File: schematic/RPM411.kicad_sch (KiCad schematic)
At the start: 88 parts, among them J1 02x08_tbd, P1 P_Cap, Q1 tbd (GDS), U1 STM32F100C8Tb8, U2 TS5A9411, U3 TS5A9411, U4 TS5A9411, U5 74LVC3G04, U6 74LVC1G32, U7 TLV70030DDC

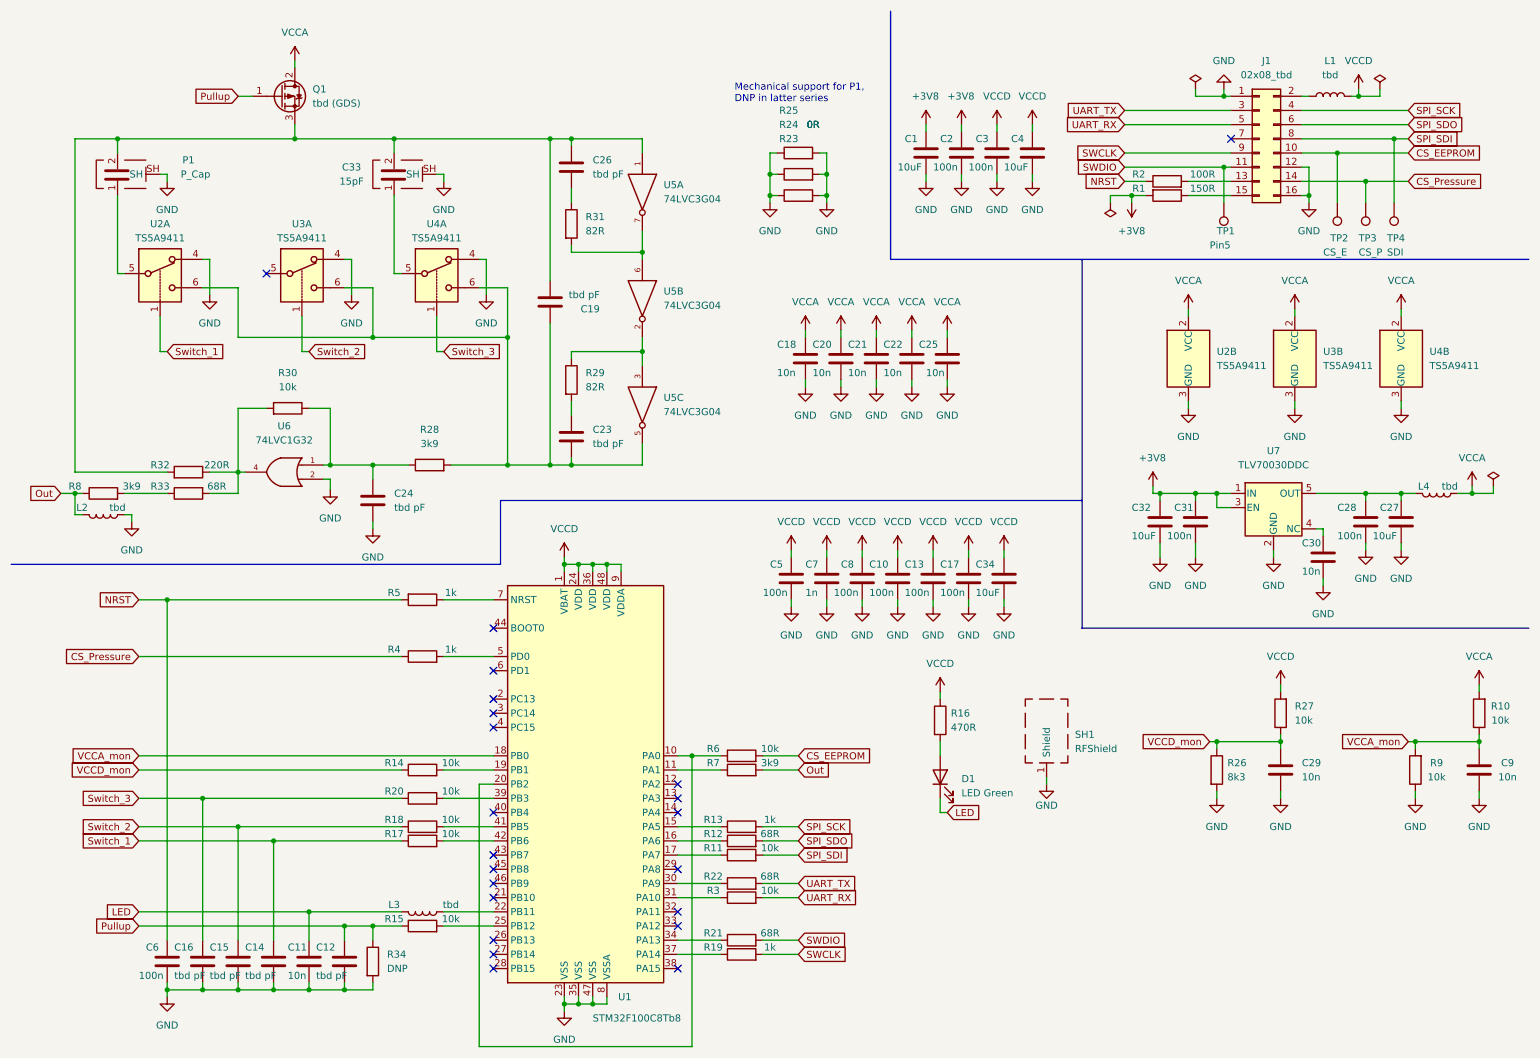
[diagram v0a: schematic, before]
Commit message: renamed CS Signals
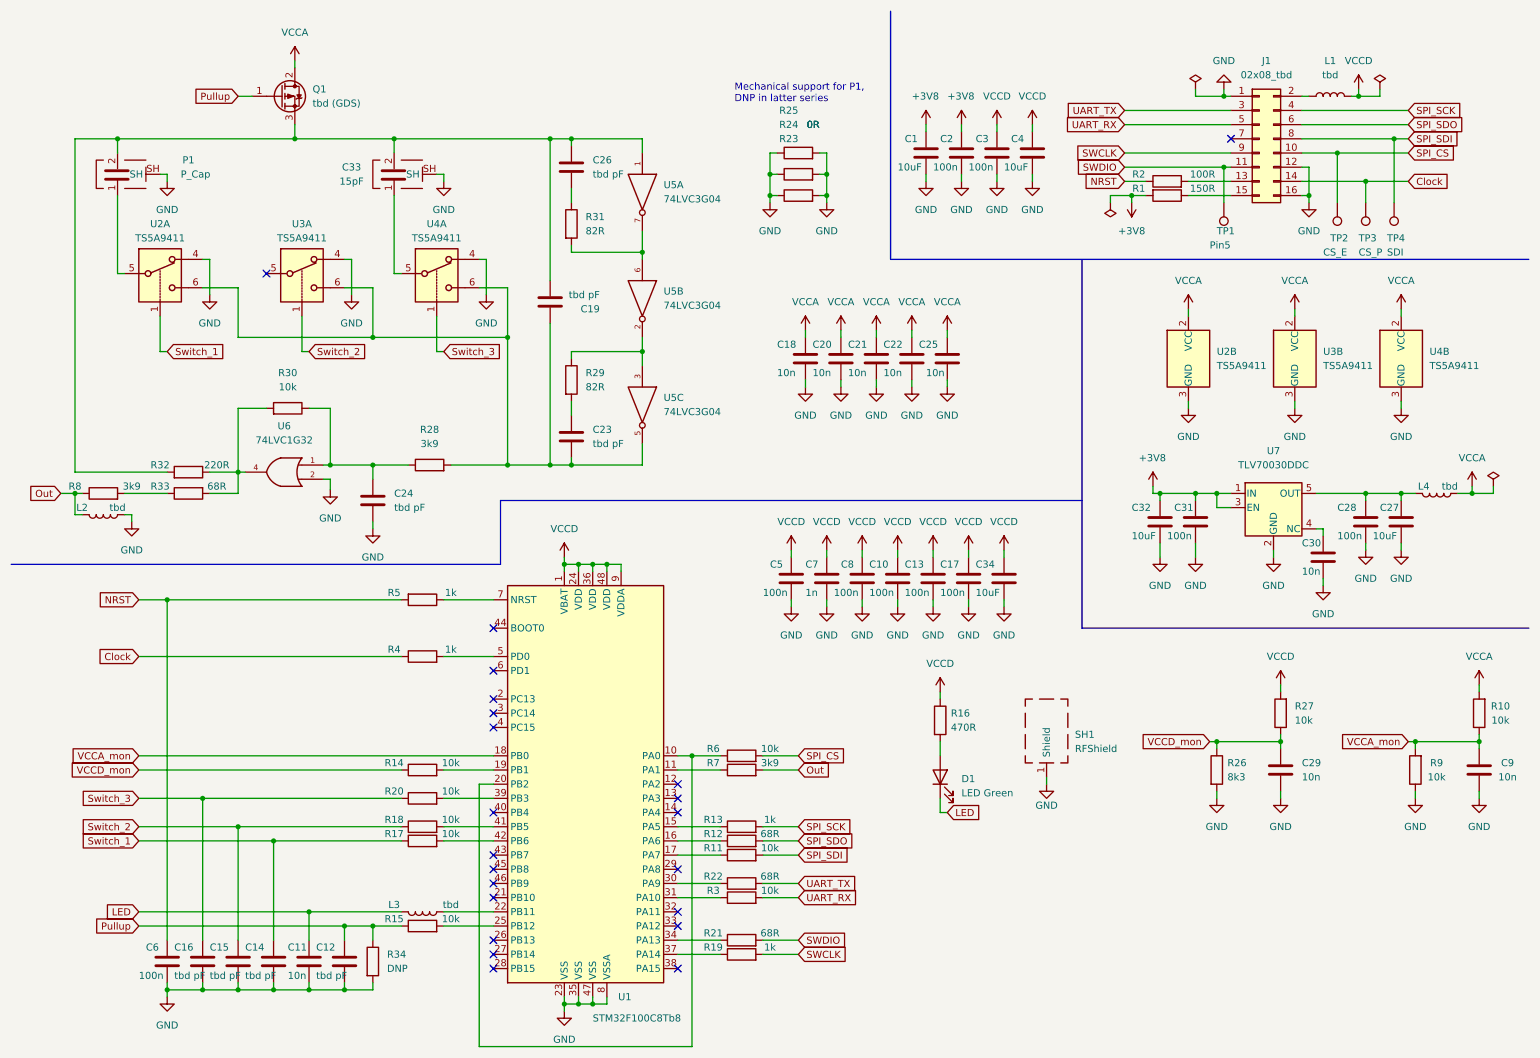
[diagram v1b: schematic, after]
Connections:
- net at U7.4 (NC): now also C30.1
- net CS_EEPROM renamed SPI_CS
- net CS_Pressure renamed Clock
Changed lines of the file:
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@@
     )
   )
-  (global_label "CS_Pressure" (shape input) (at 35.56 127 180) (fields_autoplaced)
+  (global_label "Clock" (shape input) (at 35.56 127 180) (fields_autoplaced)
     (effects (font (size 1.27 1.27)) (justify right))
     (property "Intersheet References" "${INTERSHEET_REFS}" (id 0) (at 21.475 126.9206 0)
@@
     )
   )
-  (global_label "CS_EEPROM" (shape input) (at 153.67 144.78 0) (fields_autoplaced)
+  (global_label "SPI_CS" (shape input) (at 153.67 144.78 0) (fields_autoplaced)
     (effects (font (size 1.27 1.27)) (justify left))
     (property "Intersheet References" "${INTERSHEET_REFS}" (id 0) (at 167.1502 144.7006 0)
@@
     )
   )
-  (global_label "CS_Pressure" (shape input) (at 262.89 41.91 0) (fields_autoplaced)
+  (global_label "Clock" (shape input) (at 262.89 41.91 0) (fields_autoplaced)
     (effects (font (size 1.27 1.27)) (justify left))
     (property "Intersheet References" "${INTERSHEET_REFS}" (id 0) (at 276.975 41.8306 0)
@@
     )
   )
-  (global_label "CS_EEPROM" (shape input) (at 262.89 36.83 0) (fields_autoplaced)
+  (global_label "SPI_CS" (shape input) (at 262.89 36.83 0) (fields_autoplaced)
     (effects (font (size 1.27 1.27)) (justify left))
     (property "Intersheet References" "${INTERSHEET_REFS}" (id 0) (at 276.3702 36.7506 0)
@@
     (pin "3")
     (pin "4")
+    (pin "4")
     (pin "5")
-    (pin "4")
   )
   (symbol (lib_id "power:GND") (at 184.15 118.11 0) (unit 1)
@@
       (effects (font (size 1.27 1.27)) hide)
     )
+    (pin "2")
     (pin "3")
-    (pin "2")
   )
   (symbol (lib_id "power:GND") (at 111.76 190.5 0) (unit 1)
@@
       (effects (font (size 1.27 1.27)) hide)
     )
-    (pin "6")
+    (pin "1")
     (pin "4")
     (pin "5")
-    (pin "1")
+    (pin "6")
   )
   (symbol (lib_id "power:VCC") (at 242.57 64.77 0) (unit 1)
